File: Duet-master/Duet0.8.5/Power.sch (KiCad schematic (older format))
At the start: 31 parts, among them U7 TC2117-3.3VDBTR, U8 A4403

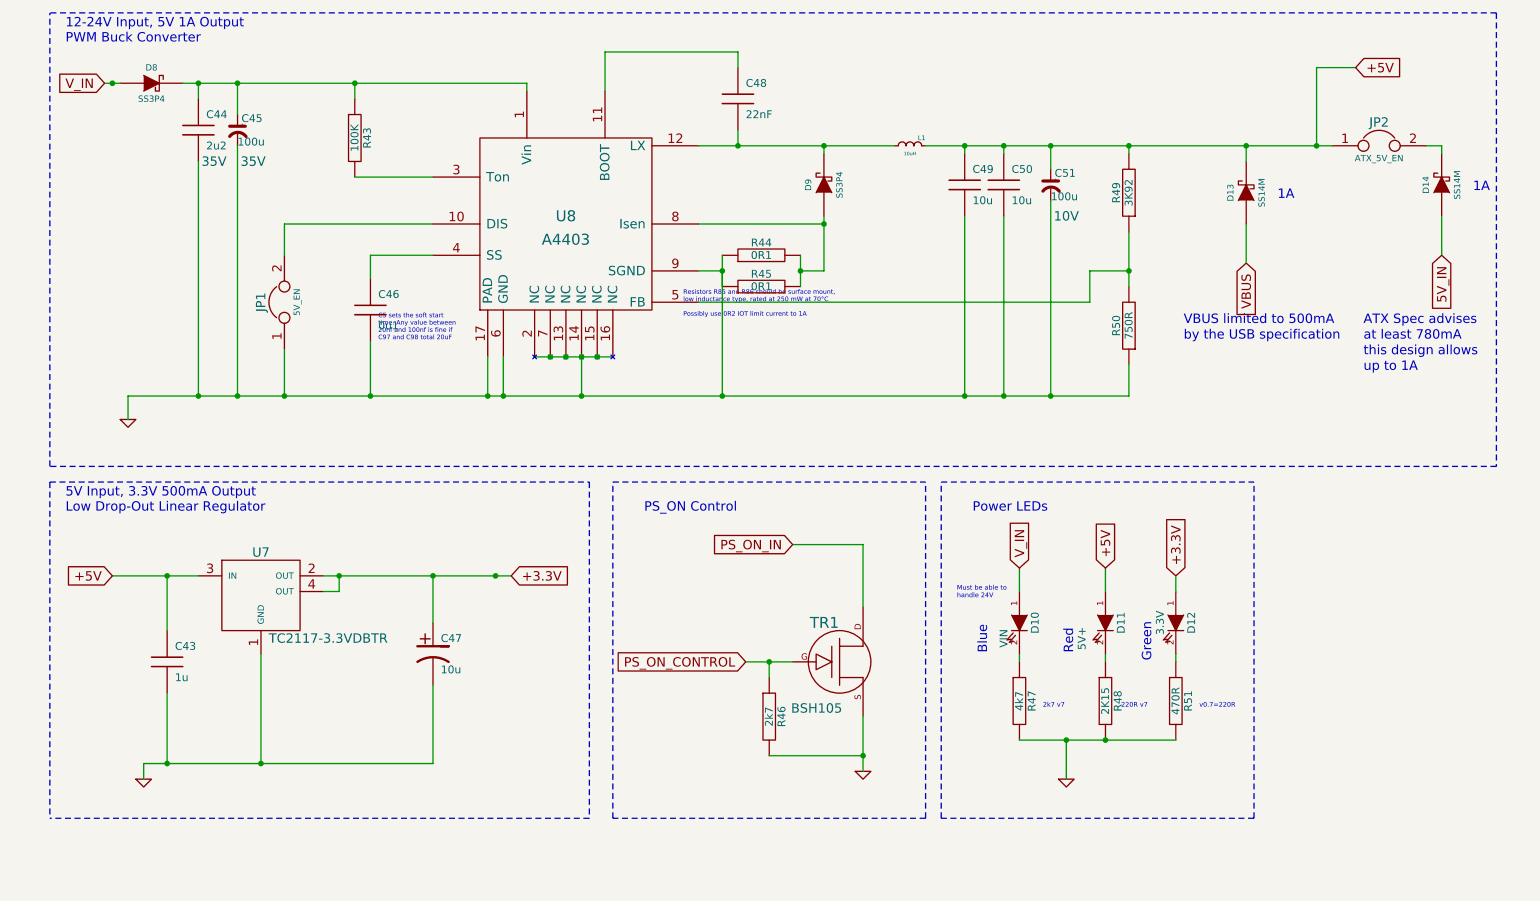
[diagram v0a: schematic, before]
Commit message: Module Library update
Lots of duplicate footprints
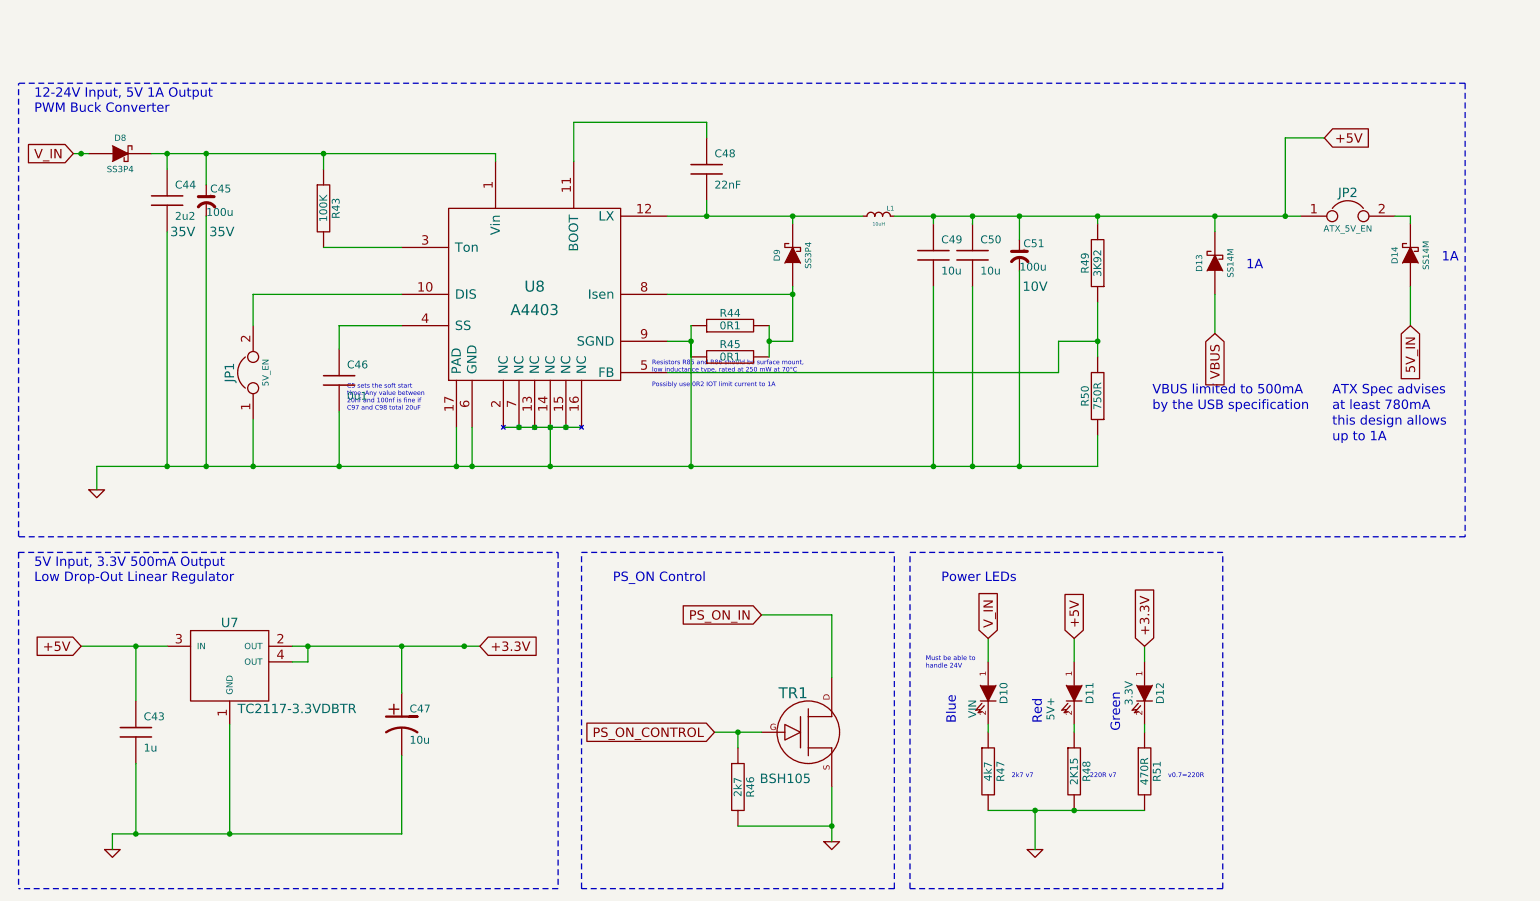
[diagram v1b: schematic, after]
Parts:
- C44: footprint (none) -> Melter_Connections:2mf2_capacitor
- C45: footprint C_ELEC_6.3x7.7 -> Melter_Connections:100mf_capacitor
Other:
- moved on the sheet: C43, C44, C45, C46, C47, C48, C49, C50, C51, D10, D11, D12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

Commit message: PCB layout of components started
Experienced advice welcome.
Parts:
- C43: footprint (none) -> Melter_Connections:1mf_capacitor
- C46: footprint (none) -> Melter_Connections:0mf1_capacitor
- C47, C49, C50: footprint (none) -> Melter_Connections:10mf_capacitor
- C48: footprint (none) -> Melter_Connections:22nf_capacitor
- C51: footprint C_ELEC_6.3x7.7 -> Melter_Connections:100mf_capacitor
- D10: footprint (none) -> Melter_Connections:V_IN_Diode_0603
- D11: footprint (none) -> Melter_Connections:5V_Diode_0603
- D12: footprint (none) -> Melter_Connections:33V_Diode_0603
- D13, D14: footprint (none) -> Melter_Connections:SS14M
- D8, D9: footprint (none) -> Melter_Connections:SS3P4
- JP1, JP2: footprint (none) -> Melter_Connections:JUMPER
- L1: footprint (none) -> Melter_Connections:10mH_L_6x6
- R43: footprint (none) -> Melter_Connections:100k_R_0603
- R44, R45: footprint (none) -> Melter_Connections:0R1_R_1206
- R46: footprint (none) -> Melter_Connections:2k7_R_0603
- R47: footprint (none) -> Melter_Connections:4k7_R_0603
- R48: footprint (none) -> Melter_Connections:2k15_R_0603
- R49: footprint (none) -> Melter_Connections:3k92_R_0603
- R50: footprint (none) -> Melter_Connections:750R_R_0603
- R51: footprint (none) -> Melter_Connections:470R_R_0603
- TR1: footprint (none) -> Melter_Connections:BSH105_SOT-23
- U7: footprint (none) -> Melter_Connections:TC2117-3.3VDBTR
- U8: footprint (none) -> Melter_Connections:A4403_QFN16-4x4
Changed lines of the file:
@@
 F 0 "C43" H 2000 5350 50  0000 L CNN
 F 1 "1u" H 2000 5150 50  0000 L CNN
-F 2 "" H 1950 5250 60  0001 C CNN
+F 2 "Melter_Connections:1mf_capacitor" H 1950 5250 60  0001 C CNN
 F 3 "" H 1950 5250 60  0001 C CNN
 	1    1950 5250
@@
 F 0 "D12" H 8400 5100 50  0000 C CNN
 F 1 "3.3V" H 8400 4900 50  0000 C CNN
-F 2 "" H 8400 5000 60  0001 C CNN
+F 2 "Melter_Connections:33V_Diode_0603" H 8400 5000 60  0001 C CNN
 F 3 "" H 8400 5000 60  0001 C CNN
 	1    8400 5000
@@
 F 0 "R51" V 8480 5500 50  0000 C CNN
 F 1 "470R" V 8400 5500 50  0000 C CNN
-F 2 "" H 8400 5500 60  0001 C CNN
+F 2 "Melter_Connections:470R_R_0603" H 8400 5500 60  0001 C CNN
 F 3 "" H 8400 5500 60  0001 C CNN
 	1    8400 5500
@@
 F 0 "D11" H 7950 5100 50  0000 C CNN
 F 1 "5V+" H 8050 4850 50  0000 C CNN
-F 2 "" H 7950 5000 60  0001 C CNN
+F 2 "Melter_Connections:5V_Diode_0603" H 7950 5000 60  0001 C CNN
 F 3 "" H 7950 5000 60  0001 C CNN
 	1    7950 5000
@@
 F 0 "R48" V 8030 5500 50  0000 C CNN
 F 1 "2K15" V 7950 5500 50  0000 C CNN
-F 2 "" H 7950 5500 60  0001 C CNN
+F 2 "Melter_Connections:2k15_R_0603" H 7950 5500 60  0001 C CNN
 F 3 "" H 7950 5500 60  0001 C CNN
 	1    7950 5500
@@
 F 0 "R47" V 7480 5500 50  0000 C CNN
 F 1 "4k7" V 7400 5500 50  0000 C CNN
-F 2 "" H 7400 5500 60  0001 C CNN
+F 2 "Melter_Connections:4k7_R_0603" H 7400 5500 60  0001 C CNN
 F 3 "" H 7400 5500 60  0001 C CNN
 	1    7400 5500
@@
 F 0 "D10" H 7400 5100 50  0000 C CNN
 F 1 "VIN" H 7500 4900 50  0000 C CNN
-F 2 "" H 7400 5000 60  0001 C CNN
+F 2 "Melter_Connections:V_IN_Diode_0603" H 7400 5000 60  0001 C CNN
 F 3 "" H 7400 5000 60  0001 C CNN
 	1    7400 5000
@@
 F 0 "R46" V 5880 5600 50  0000 C CNN
 F 1 "2k7" V 5800 5600 50  0000 C CNN
-F 2 "" H 5800 5600 60  0001 C CNN
+F 2 "Melter_Connections:2k7_R_0603" H 5800 5600 60  0001 C CNN
 F 3 "" H 5800 5600 60  0001 C CNN
 	1    5800 5600
@@
 F 0 "C47" H 3700 5300 50  0000 L CNN
 F 1 "10u" H 3700 5100 50  0000 L CNN
-F 2 "" H 3650 5200 60  0001 C CNN
+F 2 "Melter_Connections:10mf_capacitor" H 3650 5200 60  0001 C CNN
 F 3 "" H 3650 5200 60  0001 C CNN
 	1    3650 5200
@@
 F 0 "D9" H 6150 2300 40  0000 C CNN
 F 1 "SS3P4" H 6150 2100 40  0000 C CNN
-F 2 "" H 6150 2200 60  0001 C CNN
+F 2 "Melter_Connections:SS3P4" H 6150 2200 60  0001 C CNN
 F 3 "" H 6150 2200 60  0001 C CNN
 	1    6150 2200
@@
 F 0 "D14" H 10100 2300 40  0000 C CNN
 F 1 "SS14M" H 10100 2100 40  0000 C CNN
-F 2 "" H 10100 2200 60  0001 C CNN
+F 2 "Melter_Connections:SS14M" H 10100 2200 60  0001 C CNN
 F 3 "" H 10100 2200 60  0001 C CNN
 	1    10100 2200
@@
 F 0 "TR1" H 6153 5500 70  0000 C CNN
 F 1 "BSH105" H 6103 4953 60  0000 C CNN
-F 2 "" H 6250 5250 60  0001 C CNN
+F 2 "Melter_Connections:BSH105_SOT-23" H 6250 5250 60  0001 C CNN
 F 3 "" H 6250 5250 60  0001 C CNN
 	1    6250 5250
@@
 F 0 "JP2" H 9700 2100 60  0000 C CNN
 F 1 "ATX_5V_EN" H 9700 1870 40  0000 C CNN
-F 2 "" H 9700 1950 60  0001 C CNN
+F 2 "Melter_Connections:JUMPER" H 9700 1950 60  0001 C CNN
 F 3 "" H 9700 1950 60  0001 C CNN
 	1    9700 1950
@@
 F 0 "JP1" H 2700 3100 60  0000 C CNN
 F 1 "5V_EN" H 2700 2870 40  0000 C CNN
-F 2 "" H 2700 2950 60  0001 C CNN
+F 2 "Melter_Connections:JUMPER" H 2700 2950 60  0001 C CNN
 F 3 "" H 2700 2950 60  0001 C CNN
 	1    2700 2950
@@
 F 0 "D8" H 1850 1650 40  0000 C CNN
 F 1 "SS3P4" H 1850 1450 40  0000 C CNN
-F 2 "" H 1850 1550 60  0001 C CNN
+F 2 "Melter_Connections:SS3P4" H 1850 1550 60  0001 C CNN
 F 3 "" H 1850 1550 60  0001 C CNN
 	1    1850 1550
@@
 F 0 "D13" H 8850 2350 40  0000 C CNN
 F 1 "SS14M" H 8850 2150 40  0000 C CNN
-F 2 "" H 8850 2250 60  0001 C CNN
+F 2 "Melter_Connections:SS14M" H 8850 2250 60  0001 C CNN
 F 3 "" H 8850 2250 60  0001 C CNN
 	1    8850 2250
@@
 F 0 "U7" H 2550 5150 60  0000 C CNN
 F 1 "TC2117-3.3VDBTR" H 2600 4600 60  0000 L CNN
-F 2 "" H 2550 4850 60  0001 C CNN
+F 2 "Melter_Connections:TC2117-3.3VDBTR" H 2550 4850 60  0001 C CNN
 F 3 "" H 2550 4850 60  0001 C CNN
 	1    2550 4850
@@
 F 0 "C46" H 3300 3100 50  0000 L CNN
 F 1 "0u1" H 3300 2900 50  0000 L CNN
-F 2 "" H 3250 3000 60  0001 C CNN
+F 2 "Melter_Connections:0mf1_capacitor" H 3250 3000 60  0001 C CNN
 F 3 "" H 3250 3000 60  0001 C CNN
 	1    3250 3000
@@
 F 0 "C48" H 5650 1750 50  0000 L CNN
 F 1 "22nF" H 5650 1550 50  0000 L CNN
-F 2 "" H 5600 1650 60  0001 C CNN
+F 2 "Melter_Connections:22nf_capacitor" H 5600 1650 60  0001 C CNN
 F 3 "" H 5600 1650 60  0001 C CNN
 	1    5600 1650
@@
 F 0 "C50" H 7350 2300 50  0000 L CNN
 F 1 "10u" H 7350 2100 50  0000 L CNN
-F 2 "" H 7300 2200 60  0001 C CNN
+F 2 "Melter_Connections:10mf_capacitor" H 7300 2200 60  0001 C CNN
 F 3 "" H 7300 2200 60  0001 C CNN
 	1    7300 2200
@@
 F 0 "C49" H 7100 2300 50  0000 L CNN
 F 1 "10u" H 7100 2100 50  0000 L CNN
-F 2 "" H 7050 2200 60  0001 C CNN
+F 2 "Melter_Connections:10mf_capacitor" H 7050 2200 60  0001 C CNN
 F 3 "" H 7050 2200 60  0001 C CNN
 	1    7050 2200
@@
 F 0 "R43" V 3230 1900 50  0000 C CNN
 F 1 "100K" V 3150 1900 50  0000 C CNN
-F 2 "" H 3150 1900 60  0001 C CNN
+F 2 "Melter_Connections:100k_R_0603" H 3150 1900 60  0001 C CNN
 F 3 "" H 3150 1900 60  0001 C CNN
 	1    3150 1900
@@
 F 0 "R44" V 5830 2650 50  0000 C CNN
 F 1 "0R1" V 5750 2650 50  0000 C CNN
-F 2 "" H 5750 2650 60  0001 C CNN
+F 2 "Melter_Connections:0R1_R_1206" H 5750 2650 60  0001 C CNN
 F 3 "" H 5750 2650 60  0001 C CNN
 	1    5750 2650
@@
 F 0 "R49" V 8180 2250 50  0000 C CNN
 F 1 "3K92" V 8100 2250 50  0000 C CNN
-F 2 "" H 8100 2250 60  0001 C CNN
+F 2 "Melter_Connections:3k92_R_0603" H 8100 2250 60  0001 C CNN
 F 3 "" H 8100 2250 60  0001 C CNN
 	1    8100 2250
@@
 F 0 "R50" V 8180 3100 50  0000 C CNN
 F 1 "750R" V 8100 3100 50  0000 C CNN
-F 2 "" H 8100 3100 60  0001 C CNN
+F 2 "Melter_Connections:750R_R_0603" H 8100 3100 60  0001 C CNN
 F 3 "" H 8100 3100 60  0001 C CNN
 	1    8100 3100
@@
 F 0 "U8" H 4500 2500 70  0000 C CNN
 F 1 "A4403" H 4500 2350 70  0000 C CNN
-F 2 "" H 4500 2450 60  0001 C CNN
+F 2 "Melter_Connections:A4403_QFN16-4x4" H 4500 2450 60  0001 C CNN
 F 3 "" H 4500 2450 60  0000 C CNN
 	1    4500 2450
@@
 F 0 "L1" H 6625 1900 30  0000 C CNN
 F 1 "10uH" H 6700 2000 22  0000 C CNN
-F 2 "" H 6700 1950 60  0001 C CNN
+F 2 "Melter_Connections:10mH_L_6x6" H 6700 1950 60  0001 C CNN
 F 3 "" H 6700 1950 60  0000 C CNN
 	1    6700 1950
@@
 F 0 "C51" H 7625 2275 50  0000 L CNN
 F 1 "100u" H 7600 2125 50  0000 L CNN
-F 2 "C_ELEC_6.3x7.7" H 7600 2200 60  0001 C CNN
+F 2 "Melter_Connections:100mf_capacitor" H 7600 2200 60  0001 C CNN
 F 3 "" H 7600 2200 60  0000 C CNN
 F 4 "10V" H 7700 2000 60  0000 C CNN "Voltage"
@@
 F 0 "R45" V 5830 2850 50  0000 C CNN
 F 1 "0R1" V 5750 2850 50  0000 C CNN
-F 2 "" H 5750 2850 60  0001 C CNN
+F 2 "Melter_Connections:0R1_R_1206" H 5750 2850 60  0001 C CNN
 F 3 "" H 5750 2850 60  0001 C CNN
 	1    5750 2850
